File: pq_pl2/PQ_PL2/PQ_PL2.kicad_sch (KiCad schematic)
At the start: 79 parts, among them J1 BBL-110-Y-X, J2 BBL-110-Y-X, J3 BBL-110-Y-X, J4 BBL-110-Y-X, J5 U.FL-R-SMT, J6 MS-156C3, J7 MS-156C3, J8 U.FL-R-SMT, U1 LEE2-6+, U2 MAX2121, U4 LT3048, U5 LT071DBV, Y1 ECS-TXO-2016MV

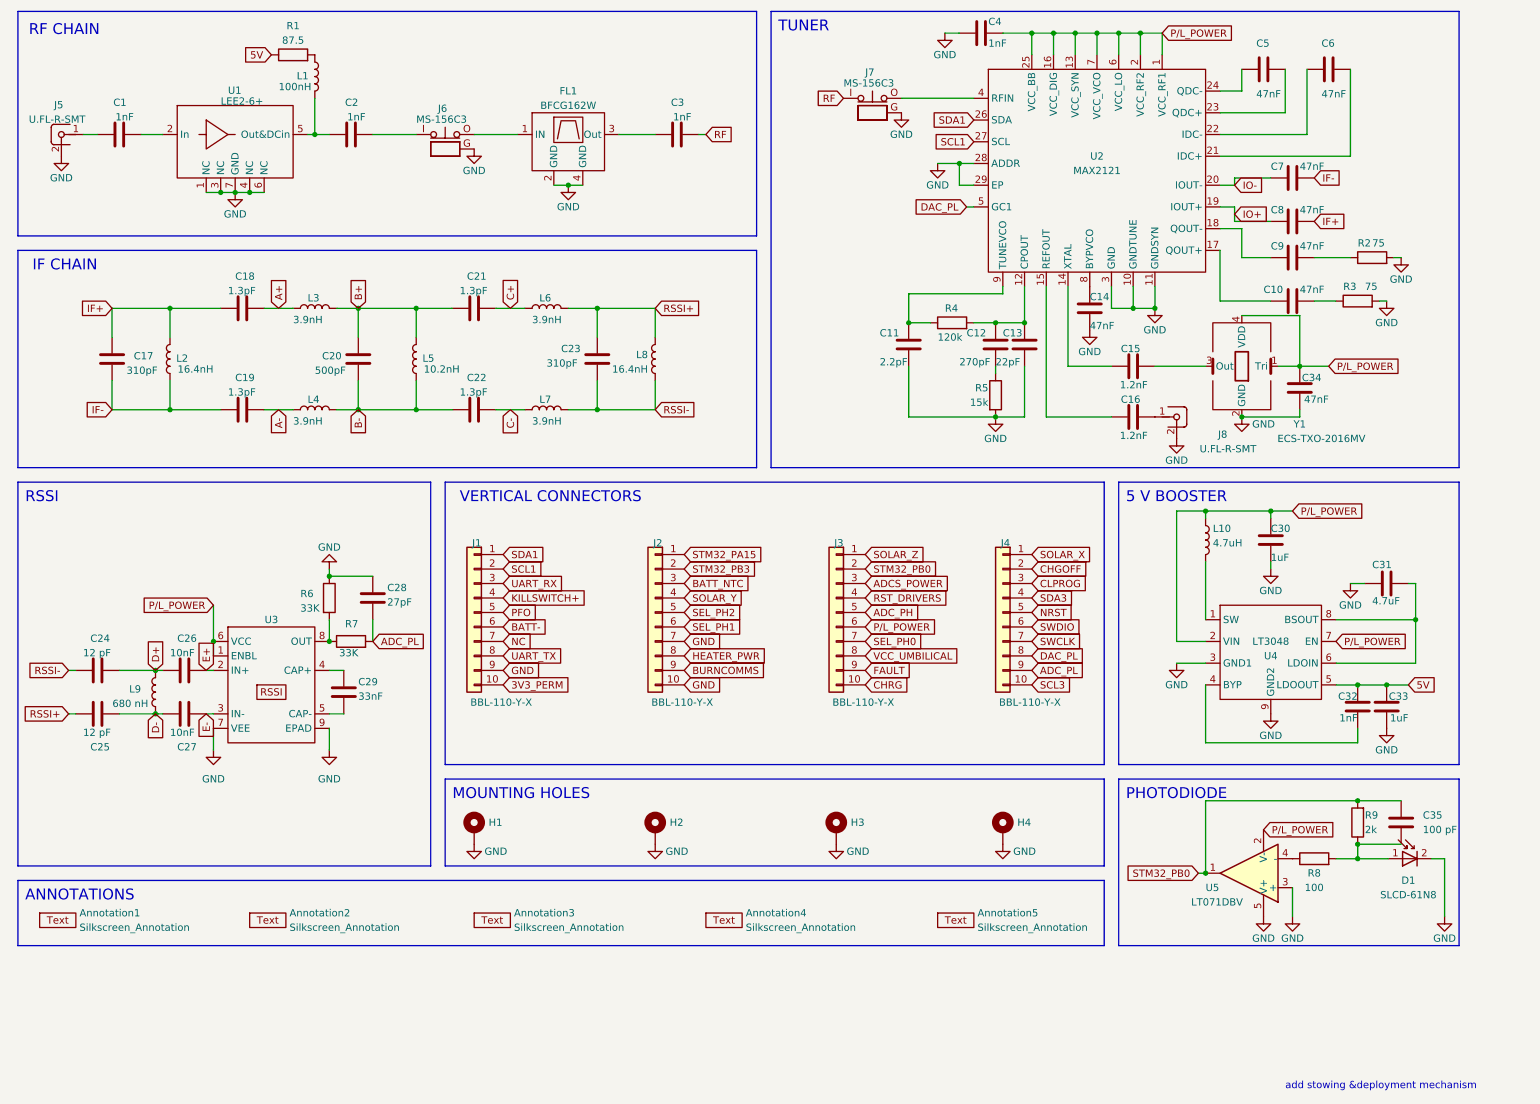
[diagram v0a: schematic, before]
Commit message: BOM creation schematic changes 2.0
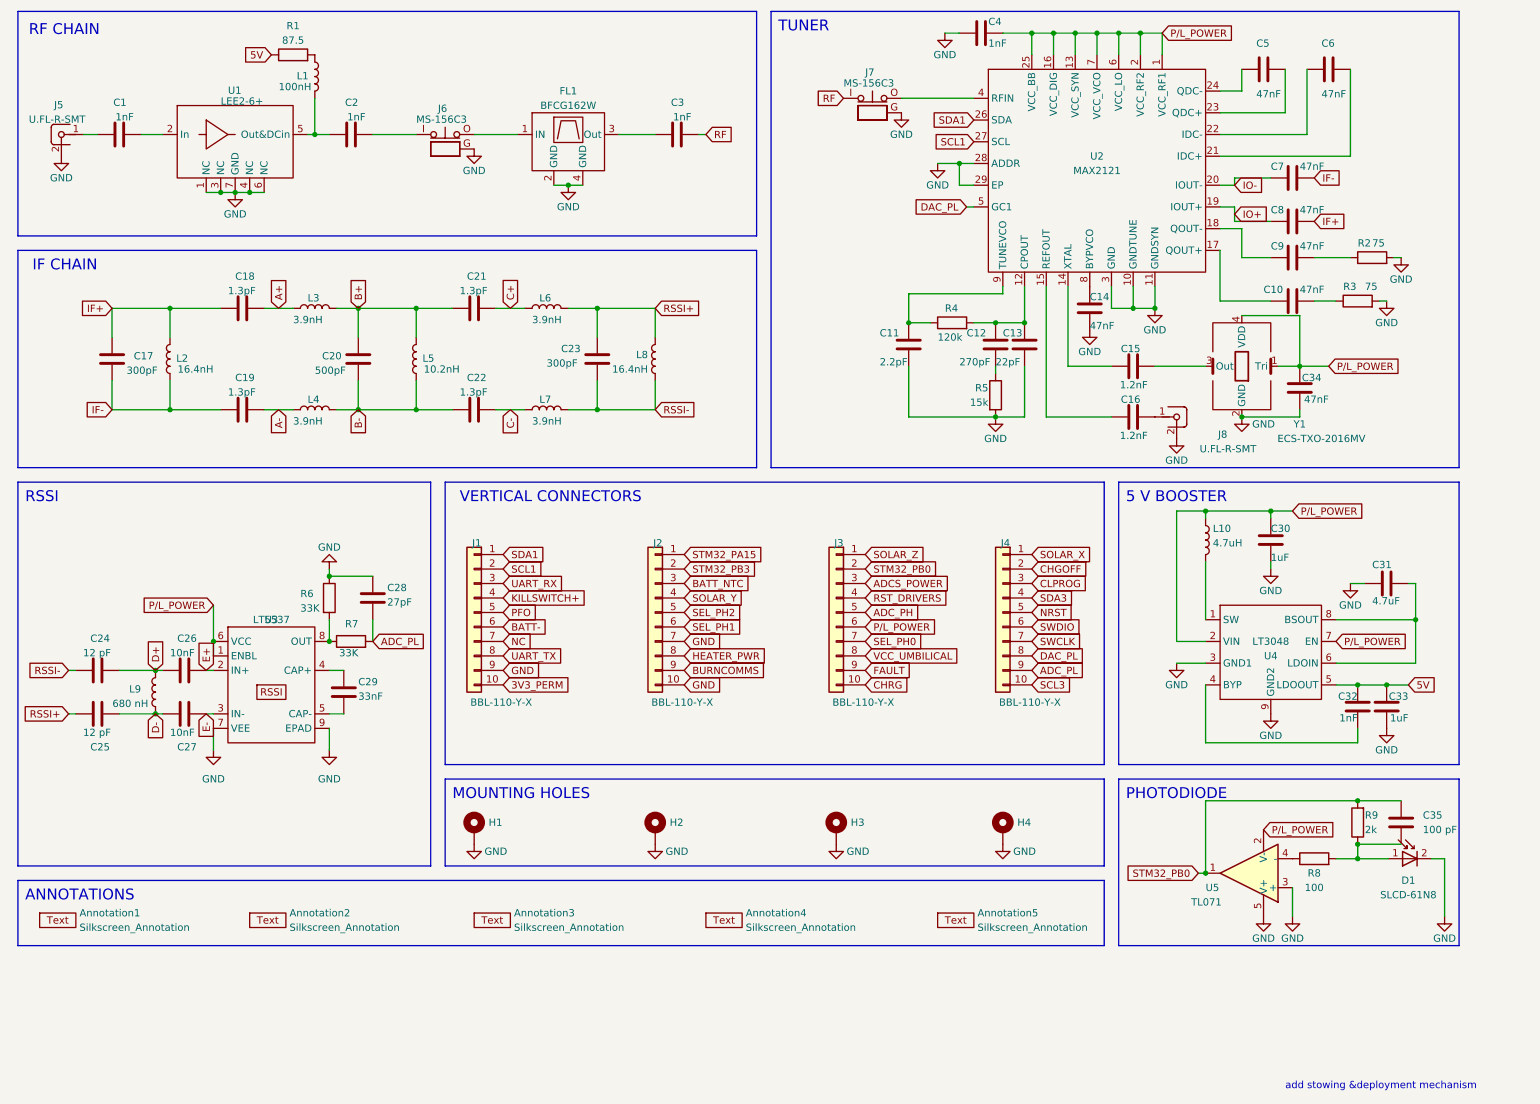
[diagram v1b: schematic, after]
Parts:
- Annotation1, Annotation2, Annotation3, Annotation4, Annotation5: Manufacturer 1 (none) -> N/A; Manufacturer Part Number 1 (none) -> N/A; Supplier 1 (none) -> N/A; Supplier Part Number 1 (none) -> N/A
- C1, C2, C3, C32, C4: Manufacturer 1 YAGEO -> Wurth Elektronik; Manufacturer Part Number 1 CC0603JRNPO0BN100 -> 885382206005; Supplier Part Number 1 (none) -> 710-885382206005
- C10, C14, C34, C5, C6, C9: Manufacturer 1 YAGEO -> TDK; Manufacturer Part Number 1 CC0603JRNPO0BN100 -> CGA3E3X7S2A473K080AE; Supplier Part Number 1 (none) -> 810-CGA3E3X7S2A473KA
- C11: Manufacturer 1 YAGEO -> KYOCERA AVX; Manufacturer Part Number 1 CC0603JRNPO0BN100 -> 06031U2R2CAT2A; Supplier Part Number 1 (none) -> 581-06031U2R2CAT2A
- C12: Manufacturer 1 YAGEO -> KYOCERA AVX; Manufacturer Part Number 1 CC0603JRNPO0BN100 -> 06031A271FAT2A; Supplier Part Number 1 (none) -> 581-06031A271FAT2A
- C13: Manufacturer 1 YAGEO -> KEMET; Manufacturer Part Number 1 CC0603JRNPO0BN100 -> CBR06C220J5GACAUTO; Supplier Part Number 1 (none) -> 80-CBR06C220J5GAUTO
- C15, C16: Manufacturer 1 YAGEO -> KEMET; Manufacturer Part Number 1 CC0603JRNPO0BN100 -> C0603C122F1GACTU; Supplier Part Number 1 (none) -> 80-C0603C122F1GACTU
- C17, C23: value 310pF -> 300pF; Manufacturer 1 YAGEO -> Murata; Manufacturer Part Number 1 CC0603JRNPO0BN100 -> GRT1555C1H301FA02D; Supplier Part Number 1 (none) -> 81-GRT1555C1H301FA2D
- C18, C19, C21, C22: Manufacturer 1 YAGEO -> KEMET; Manufacturer Part Number 1 CC0603JRNPO0BN100 -> CBR04C139A5GAC; Supplier Part Number 1 (none) -> 80-CBR04C139A5GAC
- C20: Manufacturer 1 YAGEO -> KYOCERA AVX; Manufacturer Part Number 1 CC0603JRNPO0BN100 -> 0402ZC501KAT2A; Supplier Part Number 1 (none) -> 581-0402ZC501KAT2A
- C24, C25: Manufacturer 1 YAGEO -> KEMET; Manufacturer Part Number 1 CC0603JRNPO0BN100 -> CBR04C120F2GAC; Supplier Part Number 1 (none) -> 80-CBR04C120F2GAC
- C26, C27: Manufacturer 1 YAGEO -> Murata; Manufacturer Part Number 1 CC0603JRNPO0BN100 -> GRM1555C1E103GE01D; Supplier Part Number 1 (none) -> 81-GRM1555C1E103GE1D
- C28: Manufacturer 1 Murata -> KEMET; Manufacturer Part Number 1 GRM188C80J106MA73D -> CBR04C270F2GAC; Supplier Part Number 1 (none) -> 80-CBR04C270F2GAC
- C29: Manufacturer 1 Murata -> KYOCERA AVX; Manufacturer Part Number 1 GRM188C80J106MA73D -> 0402YC333JAT2A; Supplier Part Number 1 (none) -> 581-0402YC333JAT2A
- C30, C33: Manufacturer 1 YAGEO -> TAIYO YUDEN; Manufacturer Part Number 1 CC0603JRNPO0BN100 -> MAASA105CD7105KFCA01; Supplier Part Number 1 (none) -> 963-MAASA105CD7105KF
- C31: Manufacturer 1 YAGEO -> TDK; Manufacturer Part Number 1 CC0603JRNPO0BN100 -> C1005X5R1A475K050BC; Supplier Part Number 1 (none) -> 810-C1005X5R1A475KBC
- C7, C8: Manufacturer 1 YAGEO -> TAIYO YUDEN; Manufacturer Part Number 1 CC0603JRNPO0BN100 -> MAASU105SB7473KFCA01; Supplier Part Number 1 (none) -> 963-MAASU105SB7473KF
- D1: Manufacturer 1 (none) -> Advanced Photonix; Manufacturer Part Number 1 (none) -> SLCD-61N8; Supplier 1 Mouser -> Farnell; Supplier Part Number 1 (none) -> 1218991
- FL1: Manufacturer 1 (none) -> Mini-Circuits; Manufacturer Part Number 1 (none) -> BFCG-162W+; Supplier Part Number 1 (none) -> 139-BFCG-162W
- H1, H2, H3, H4: Manufacturer 1 (none) -> N/A; Manufacturer Part Number 1 (none) -> N/A; Supplier 1 Mouser -> N/A; Supplier Part Number 1 (none) -> N/A
- J1, J2, J3, J4: Manufacturer 1 (none) -> Samtec; Manufacturer Part Number 1 (none) -> BBL-110-Y-X; Supplier Part Number 1 (none) -> 200-BBL110GF
- J5, J8: Manufacturer 1 HRS -> Hirose; Supplier Part Number 1 (none) -> 798-CFL-R-SMT-190
- J6, J7: Manufacturer 1 HRS(广濑) -> Hirose; Supplier Part Number 1 (none) -> 798-MS-156C3
- L1: Manufacturer 1 Sunlord -> Wurth Elektronik; Manufacturer Part Number 1 SDFL1005LR10KTF -> 7447860210G; Supplier Part Number 1 C576799 -> 710-7447860210G
- L10: Manufacturer 1 Sunlord -> TDK; Manufacturer Part Number 1 SDFL1005LR10KTF -> MLF1608A3R3JTD25; Supplier Part Number 1 C576799 -> 810-MLF1608A3R3JTD25
- L2, L8: Manufacturer 1 Sunlord -> Murata; Manufacturer Part Number 1 SDFL1005LR10KTF -> LQG15WZ16NG02D; Supplier Part Number 1 C576799 -> 81-LQG15WZ16NG02D
- L3, L4, L6, L7: Manufacturer 1 Sunlord -> Murata; Manufacturer Part Number 1 SDFL1005LR10KTF -> LQW15AN3N9G80D; Supplier Part Number 1 C576799 -> 81-LQW15AN3N9G80D
- L5: Manufacturer 1 Sunlord -> Murata; Manufacturer Part Number 1 SDFL1005LR10KTF -> LQG15WZ10NG02D; Supplier Part Number 1 C576799 -> 81-LQG15WZ10NG02D
- L9: Manufacturer 1 Sunlord -> TDK; Manufacturer Part Number 1 SDFL1005LR10KTF -> MLF1005GR68KT000; Supplier Part Number 1 C576799 -> 810-MLF1005GR68KT000
- R1: Manufacturer 1 (none) -> Panasonic; Manufacturer Part Number 1 (none) -> ERA-3AEB86R6V; Supplier Part Number 1 C576799 -> 667-ERA-3AEB86R6V
- R2, R3: Manufacturer 1 (none) -> Vishay/Dale; Manufacturer Part Number 1 (none) -> TNPU060375R0BZEN0; Supplier Part Number 1 C576799 -> 71-TNPU060375R0BZEN0
- R4: Manufacturer 1 (none) -> Vishay/Dale; Manufacturer Part Number 1 (none) -> TNPW0603120KBYEN; Supplier Part Number 1 C576799 -> 71-TNPW0603120KBYEN
- R5: Manufacturer 1 (none) -> YAGEO; Manufacturer Part Number 1 (none) -> RP0603BRD0715KL; Supplier Part Number 1 C576799 -> 603-RP0603BRD0715KL
- R6, R7: Manufacturer 1 Walsin Tech Corp -> YAGEO; Manufacturer Part Number 1 WR06X243 JTL -> RP0603BRD0733KL; Supplier Part Number 1 C576799 -> 603-RP0603BRD0733KL
- R8: Manufacturer Part Number 1 AC0603FR-13100RL -> RP0603BRD07100RL; Supplier Part Number 1 C469533 -> 603-RP0603BRD07100RL
- R9: Manufacturer Part Number 1 RC0603FR-132KL -> RP0603BRD072KL; Supplier Part Number 1 C469533 -> 603-RP0603BRD072KL
- U1: Manufacturer 1 (none) -> MiniCircuits; Manufacturer Part Number 1 (none) -> LEE2-6+; Supplier 1 MiniCircuits -> Mouser; Supplier Part Number 1 C576799 -> 139-LEE2-6
- U2: Manufacturer 1 (none) -> Analog Devices; Manufacturer Part Number 1 (none) -> MAX2121; Supplier 1 MiniCircuits -> Mouser; Supplier Part Number 1 C576799 -> 700-MAX2121ETI+
- U3: value ~ -> LT5537; Manufacturer 1 (none) -> Analog Devices; Manufacturer Part Number 1 (none) -> LT5537; Supplier Part Number 1 (none) -> 584-LT5537EDDB#TRPBF
- U4: Manufacturer 1 (none) -> Analog Devices; Manufacturer Part Number 1 (none) -> LT3048; Supplier Part Number 1 (none) -> 584-LT3048IDC#TRPBF
- U5: value LT071DBV -> TL071; Manufacturer 1 (none) -> Texas Instruments; Manufacturer Part Number 1 (none) -> TL071; Supplier Part Number 1 (none) -> 595-TL071HIDCKR
- Y1: Manufacturer 1 (none) -> ECS; Manufacturer Part Number 1 (none) -> ECS-TXO-2016MV; Supplier Part Number 1 (none) -> 520-TXO-2016MV-160TR

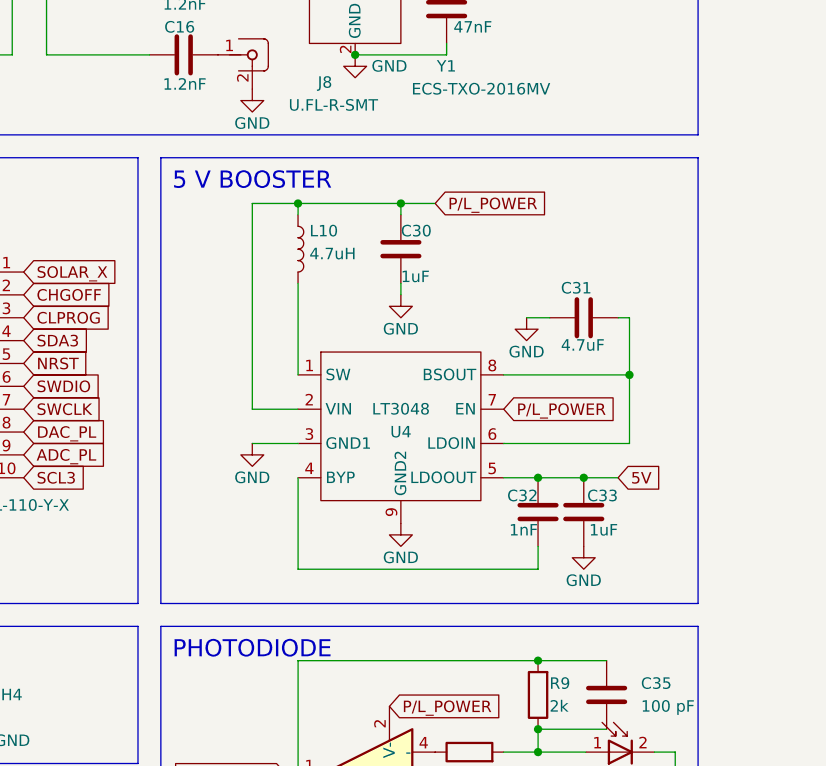
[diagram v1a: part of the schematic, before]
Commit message: Corrected the PL2 5V booster issue (changed the pins of the LT3048-5 to LT3048 & added resistive divider for 5V output)
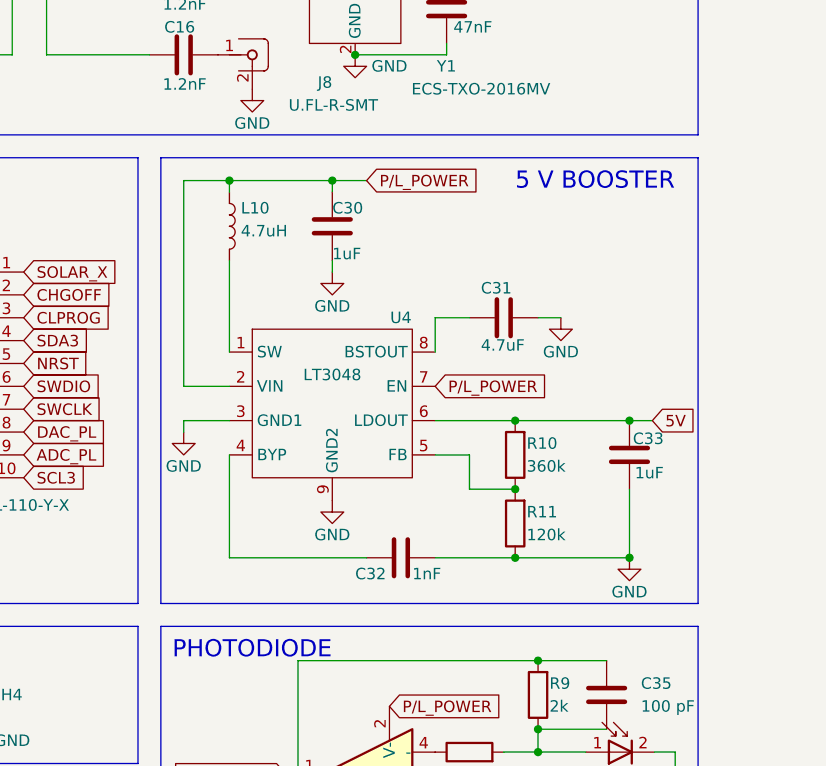
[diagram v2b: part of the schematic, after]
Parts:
- added R10: 360k, Resistor_SMD:R_0603_1608Metric, symbol Device:R
- added R11: 120k, Resistor_SMD:R_0603_1608Metric, symbol Device:R
- U4: symbol -nsl_power:LT3048 -> power-nsl:LT3048
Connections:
- net 5V: now also U4.6 (LDOUT), R10.2; no longer C32.2, U4.5 (LDOOUT)
- net GND: now also C31.1, C32.1, R11.1; no longer C31.2
- net at U4.4 (BYP): now also C32.2; no longer C32.1
- new net: R10.1, R11.2, U4.5 (FB)
- new net: C31.2, U4.8 (BSTOUT)
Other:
- moved on the sheet: C30, C31, C32, C33, L10, U4
